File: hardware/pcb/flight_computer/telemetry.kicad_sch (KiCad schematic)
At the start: 3 parts, among them J1 NRF24L01

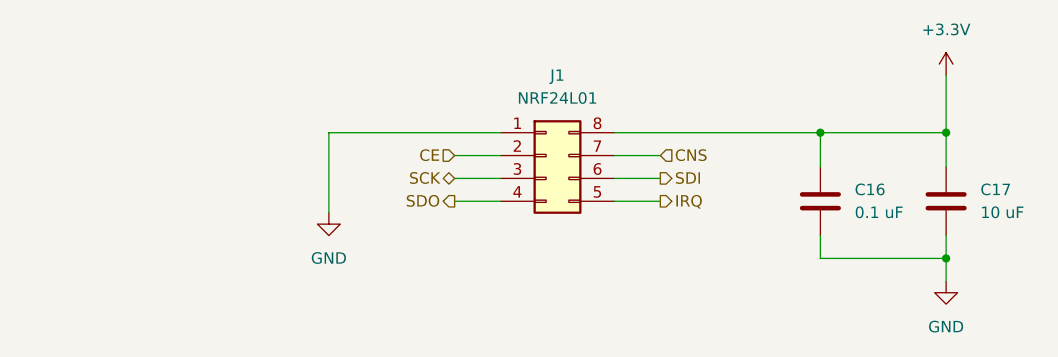
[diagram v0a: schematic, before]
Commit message: Consolidate simulation and hardware into single ember repo
Absorb the standalone simulation repo into ember as plain files,
add root .gitignore, and update hardware CAD assets.

Co-Authored-By: Claude Opus 4.8 <noreply@anthropic.com>
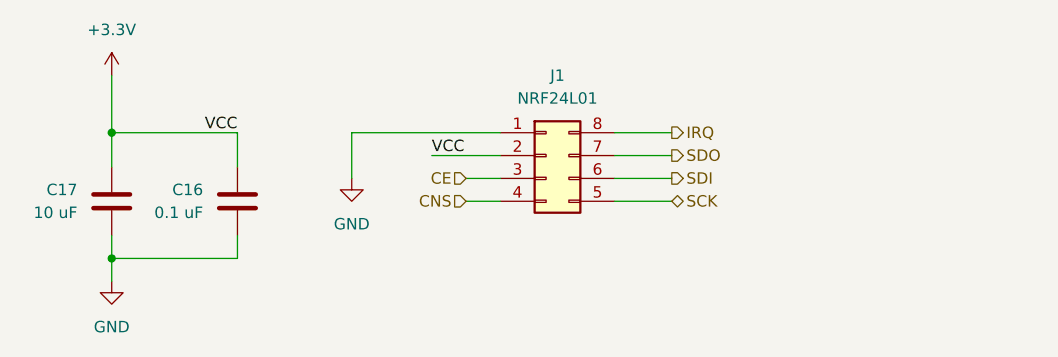
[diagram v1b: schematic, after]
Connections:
- net +3.3V: now also J1.2 (Pin_2); no longer J1.8 (Pin_8)
- net CE: now also J1.3 (Pin_3); no longer J1.2 (Pin_2)
- net CNS: now also J1.4 (Pin_4); no longer J1.7 (Pin_7)
- net IRQ: now also J1.8 (Pin_8); no longer J1.5 (Pin_5)
- net SCK: now also J1.5 (Pin_5); no longer J1.3 (Pin_3)
- net SDO: now also J1.7 (Pin_7); no longer J1.4 (Pin_4)
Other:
- moved on the sheet: C16, C17
